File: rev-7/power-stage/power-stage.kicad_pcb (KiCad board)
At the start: 6 copper layers, 40 x 39.5 mm, 142 parts, among them J1 10132797-021100LF, J2 10132797-021100LF, J3 10132797-021100LF, J4 Motor, Q1 LMG5200, Q2 LMG5200, Q3 LMG5200, U1 AS5047P, U2 INA240A1PW, U3 INA240A1PW, U4 INA240A1PW

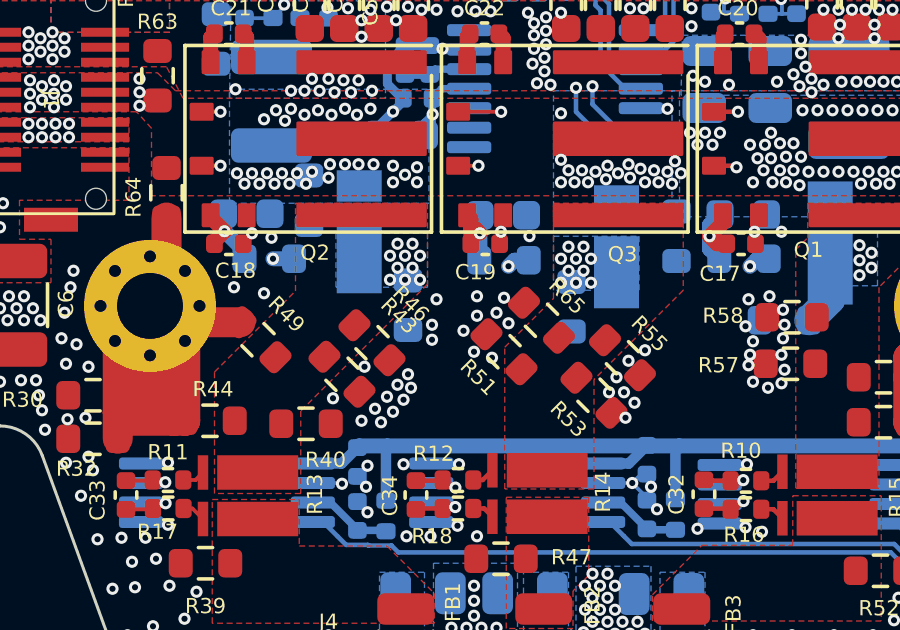
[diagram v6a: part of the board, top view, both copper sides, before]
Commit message: unfucked via, added text note
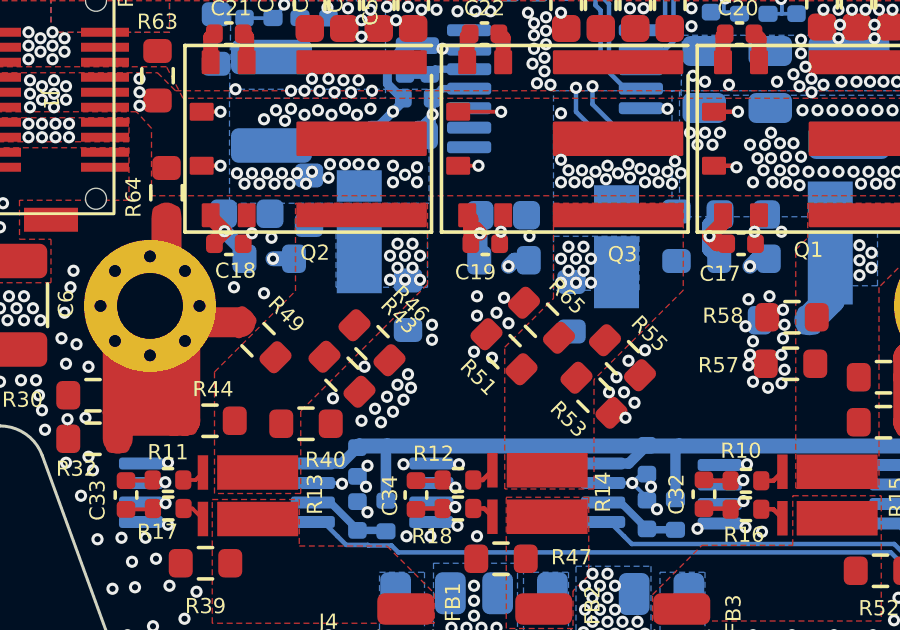
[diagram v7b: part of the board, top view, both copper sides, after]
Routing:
- net GND: vias 447 -> 445
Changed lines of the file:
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@@
     (fp_arc (start 19.999999 13.223079) (mid 19.560659 14.283739) (end 18.499999 14.723079) (layer "Edge.Cuts") (width 0.1))
     (fp_arc (start -12.759676 24.723079) (mid -13.620049 24.451819) (end -14.169215 23.736109) (layer "Edge.Cuts") (width 0.1))
-    (fp_arc (start 15.772948 -14.776921) (mid 16.561544 -14.552897) (end 17.114589 -13.947741) (layer "Edge.Cuts") (width 0.1))
-    (fp_arc (start 19.84164 -8.493639) (mid 19.959871 -8.167449) (end 19.999999 -7.822819) (layer "Edge.Cuts") (width 0.1))
+    (fp_arc (start 15.772948 -14.776921) (mid 16.561546 -14.552898) (end 17.114589 -13.947741) (layer "Edge.Cuts") (width 0.1))
+    (fp_arc (start 19.84164 -8.493639) (mid 19.959877 -8.167449) (end 19.999999 -7.822819) (layer "Edge.Cuts") (width 0.1))
     (fp_arc (start 14.169213 23.736109) (mid 13.62004 24.451806) (end 12.759674 24.723079) (layer "Edge.Cuts") (width 0.1))
     (fp_arc (start -17.114591 -13.947741) (mid -16.561547 -14.552897) (end -15.77295 -14.776921) (layer "Edge.Cuts") (width 0.1))
@@
   (via (at 85.55 56.35) (size 0.4064) (drill 0.2032) (layers "F.Cu" "B.Cu") (free) (net 2))
   (via (at 114.25 61.15) (size 0.4064) (drill 0.2032) (layers "F.Cu" "B.Cu") (free) (net 2))
-  (via (at 94.25 75.45) (size 0.4064) (drill 0.2032) (layers "F.Cu" "B.Cu") (free) (net 2))
   (via (at 109.7 86.45) (size 0.4064) (drill 0.2032) (layers "F.Cu" "B.Cu") (free) (net 2))
   (via (at 95.6 74.35) (size 0.4064) (drill 0.2032) (layers "F.Cu" "B.Cu") (free) (net 2))
@@
   (via (at 88.05 50.85) (size 0.4064) (drill 0.2032) (layers "F.Cu" "B.Cu") (free) (net 2))
   (via (at 115.4 63.6) (size 0.4064) (drill 0.2032) (layers "F.Cu" "B.Cu") (free) (net 2))
-  (via (at 93.35 74.4) (size 0.4064) (drill 0.2032) (layers "F.Cu" "B.Cu") (free) (net 2))
   (via (at 107.4 88) (size 0.4064) (drill 0.2032) (layers "F.Cu" "B.Cu") (free) (net 2))
   (via (at 114.2 77.7) (size 0.4064) (drill 0.2032) (layers "F.Cu" "B.Cu") (free) (net 2))

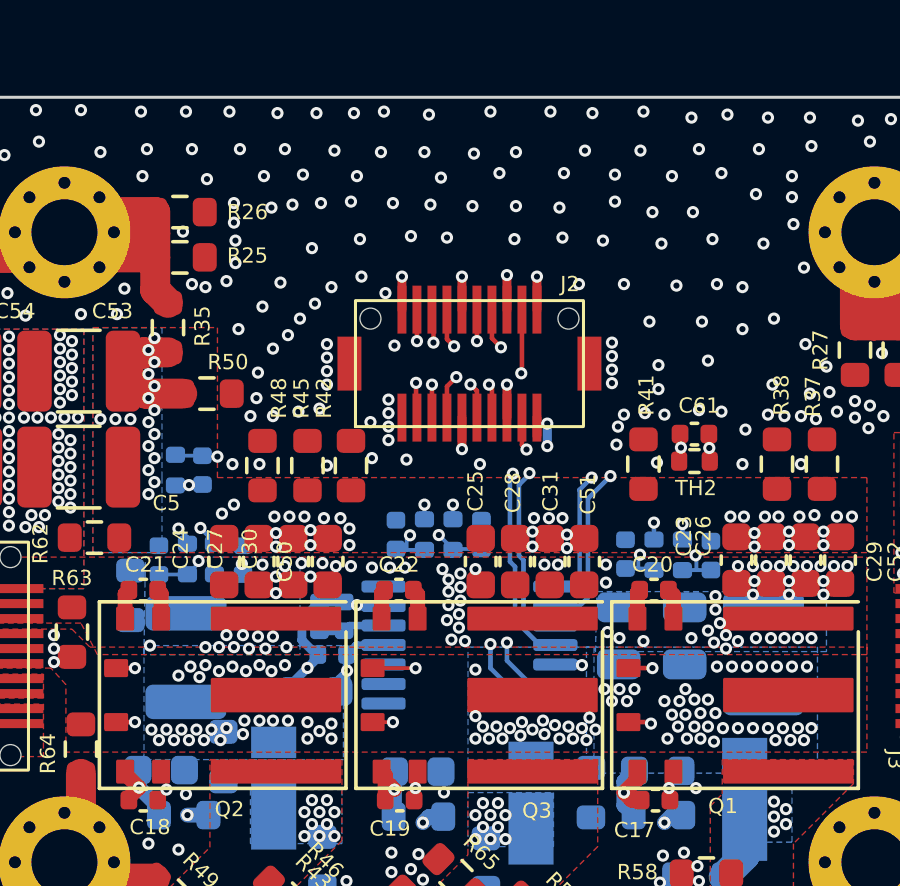
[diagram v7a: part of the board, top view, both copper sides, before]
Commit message: Switch to running mag encoder on 3v3, move to OResat standard debug connector
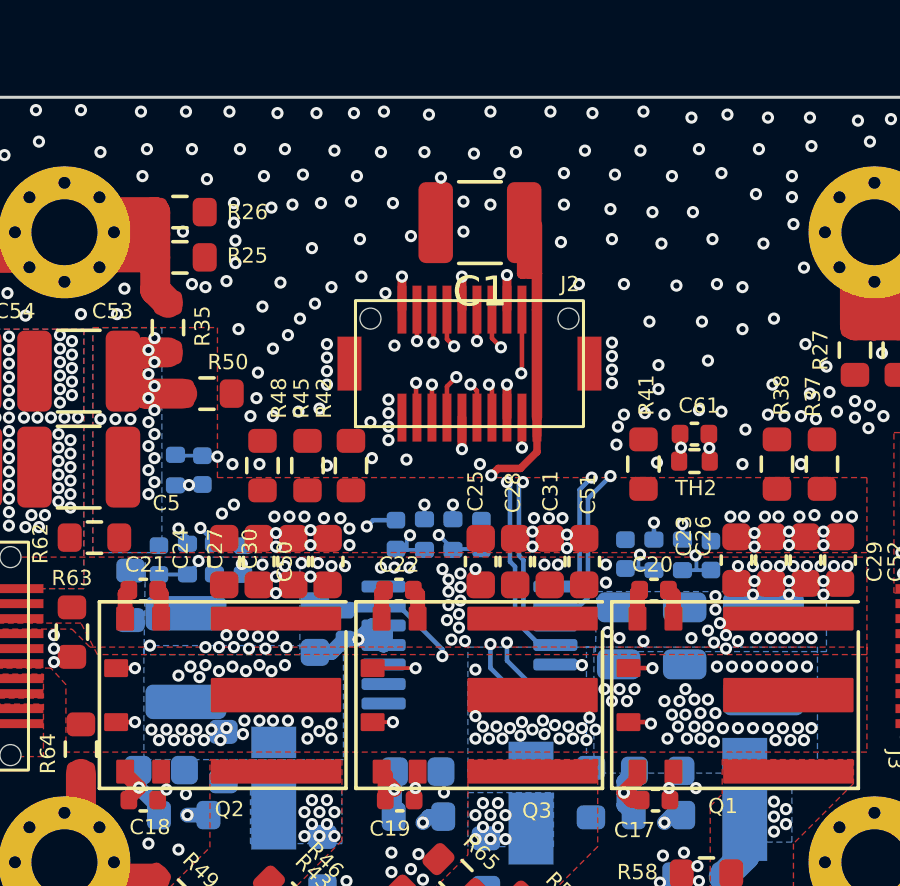
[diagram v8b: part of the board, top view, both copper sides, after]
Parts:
- removed C2: 100n, Capacitor_SMD:C_0402_1005Metric
- C1: value 1u -> 47u; footprint Capacitor_SMD:C_0402_1005Metric -> Capacitor_SMD:C_1210_3225Metric; moved to F.Cu
- moved C1 14.2 mm to (97.7, 53.3), turned to 180 degrees
- moved C3 2.08 mm to (92.2, 66.8), turned to 90 degrees
- moved C4 1.09 mm to (93.2, 66.7), turned to 90 degrees
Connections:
- C1 pad 1: Net-(C1-Pad1) -> +3V3
- C3 pad 1: +5V -> +3V3
- C4 pad 1: +5V -> +3V3
- J2 pad 10: GND -> +3V3
- J2 pad 11: GND -> +3V3
- U1 pad 11: +5V -> +3V3
- U1 pad 12: Net-(C1-Pad1) -> +3V3
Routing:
- net +3V3: track 0.00 -> 29.5 mm, vias 0 -> 2
- net +5V: track 8.91 -> 2.19 mm, vias 12 -> 11
- net Net-(C1-Pad1): track 2.21 -> 0.00 mm
- net GND: track 34.4 -> 32.4 mm, vias 445 -> 440
